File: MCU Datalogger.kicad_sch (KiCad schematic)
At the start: 0 parts

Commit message: Added required Symbols to the schematic sheets
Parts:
- added BT1: Battery, symbol Device:Battery
- added C1, C2, C3, C4: C, symbol Device:C
- added C5: C_Polarized, symbol Device:C_Polarized
- added D1, D2: LED, symbol Device:LED
- added H1, H2, H3, H4: MountingHole, symbol Mechanical:MountingHole
- added R1, R2, R3, R4, R5, R6, R7: R, symbol Device:R
- added U1, U2: 24LC1025, symbol Memory_EEPROM:24LC1025
- added U3: DS1337S_, DS1337S_:SOIC127P600X175-8N, symbol DS1337S:DS1337S_
- added U4: ATMEGA328P-AU, ATMEGA328P-AU:QFP80P900X900X120-32N, symbol ATMEGA328P-AU:ATMEGA328P-AU
- added Y1, Y2: Crystal, symbol Device:Crystal
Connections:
- new net: U4.21 (GND), U4.3 (GND), U4.5 (GND)
- new net: U4.4 (VCC), U4.6 (VCC)
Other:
- added sheet Connectors (connectors.kicad_sch)

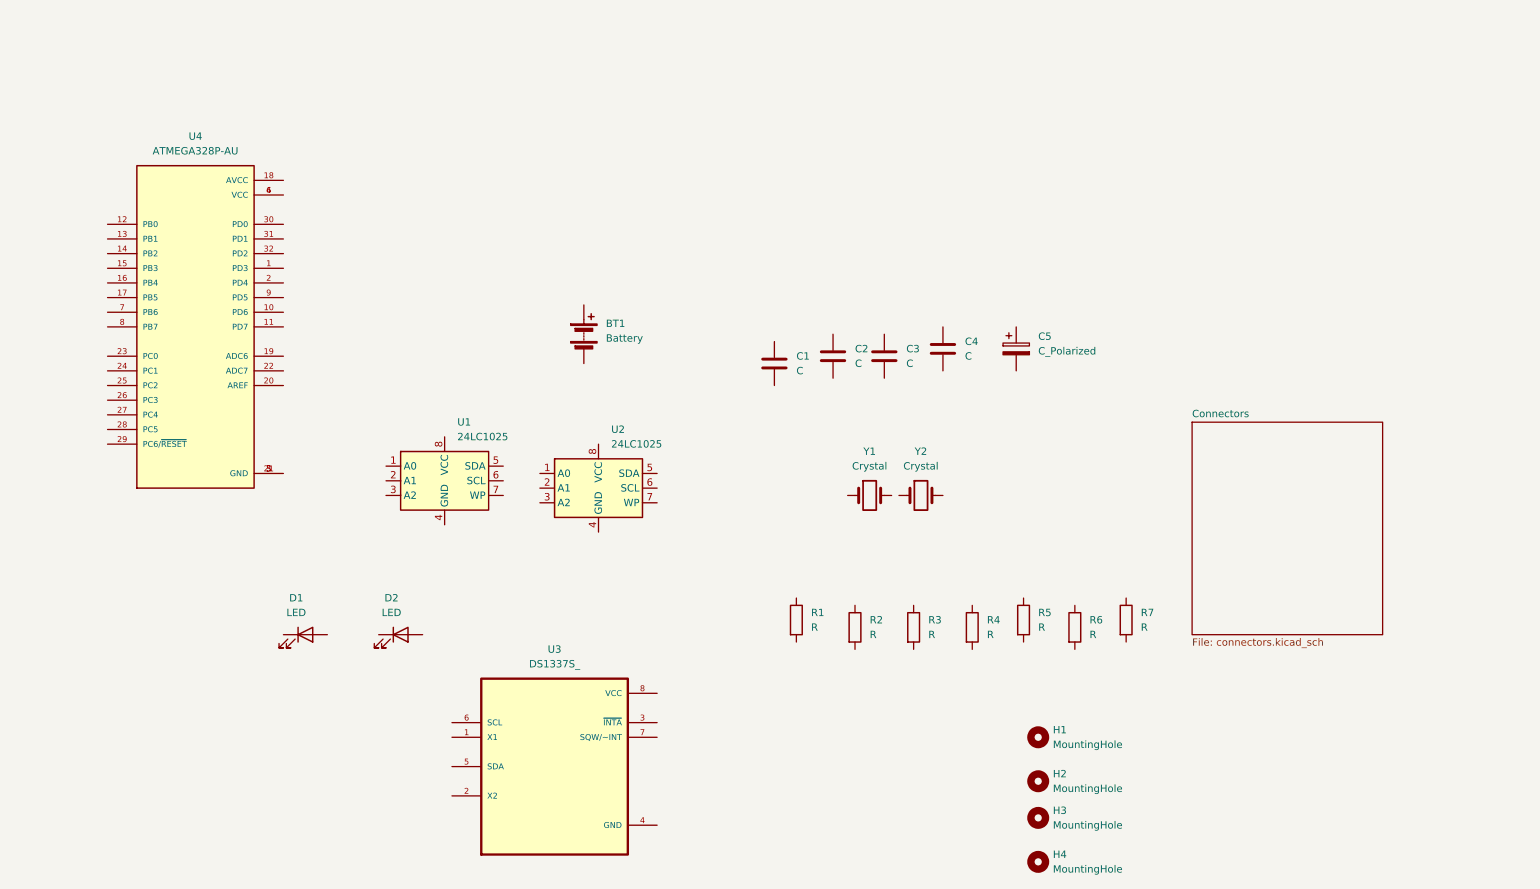
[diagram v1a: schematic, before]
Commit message: completed symbol-footprint associations
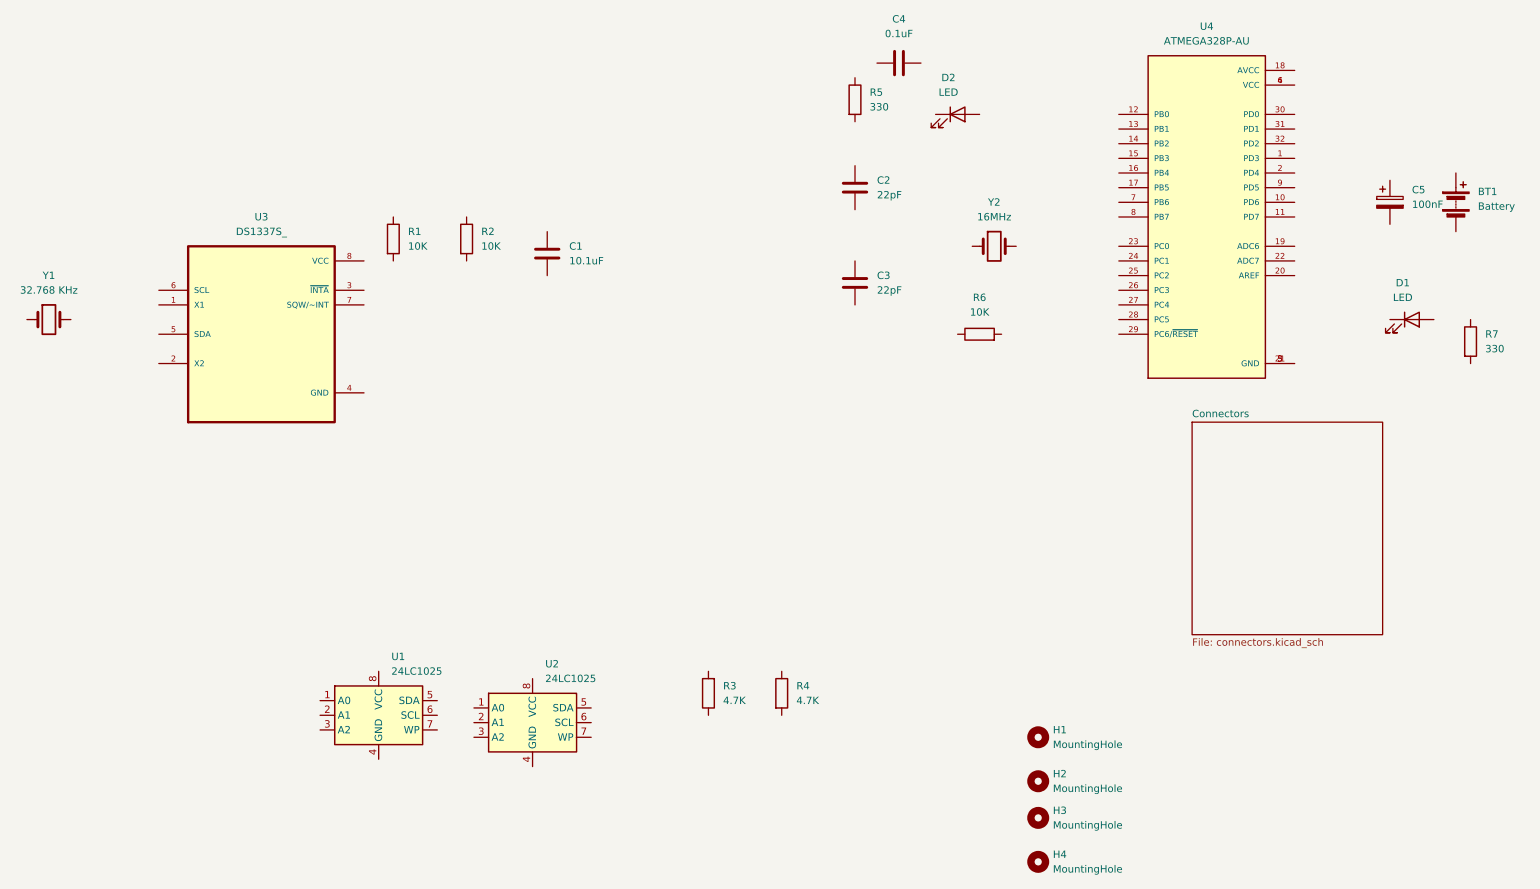
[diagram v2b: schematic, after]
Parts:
- BT1: footprint (none) -> Connector_PinHeader_2.54mm:PinHeader_1x02_P2.54mm_Vertical
- C1: value C -> 10.1uF; footprint (none) -> Capacitor_SMD:C_0805_2012Metric_Pad1.18x1.45mm_HandSolder
- C2, C3: value C -> 22pF; footprint (none) -> Capacitor_SMD:C_0805_2012Metric_Pad1.18x1.45mm_HandSolder
- C4: value C -> 0.1uF; footprint (none) -> Capacitor_SMD:C_0805_2012Metric_Pad1.18x1.45mm_HandSolder
- C5: value C_Polarized -> 100nF; footprint (none) -> Capacitor_SMD:C_0805_2012Metric_Pad1.18x1.45mm_HandSolder
- D1, D2: footprint (none) -> LED_SMD:LED_0805_2012Metric_Pad1.15x1.40mm_HandSolder
- H1, H2, H3, H4: footprint (none) -> MountingHole:MountingHole_2.2mm_M2
- R1, R2, R6: value R -> 10K; footprint (none) -> Resistor_SMD:R_0805_2012Metric_Pad1.20x1.40mm_HandSolder
- R3, R4: value R -> 4.7K; footprint (none) -> Resistor_SMD:R_0805_2012Metric_Pad1.20x1.40mm_HandSolder
- R5, R7: value R -> 330; footprint (none) -> Resistor_SMD:R_0805_2012Metric_Pad1.20x1.40mm_HandSolder
- U1, U2: footprint (none) -> Package_SO:SOIC-8_3.9x4.9mm_P1.27mm
- Y1: value Crystal -> 32.768 KHz; footprint (none) -> Crystal:Crystal_SMD_5032-2Pin_5.0x3.2mm_HandSoldering
- Y2: value Crystal -> 16MHz; footprint (none) -> Crystal:Crystal_SMD_5032-2Pin_5.0x3.2mm_HandSoldering
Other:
- moved on the sheet: BT1, C1, C2, C3, C4, C5, D1, D2, R1, R2, R3, R4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
